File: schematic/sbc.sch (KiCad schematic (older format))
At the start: 5 parts

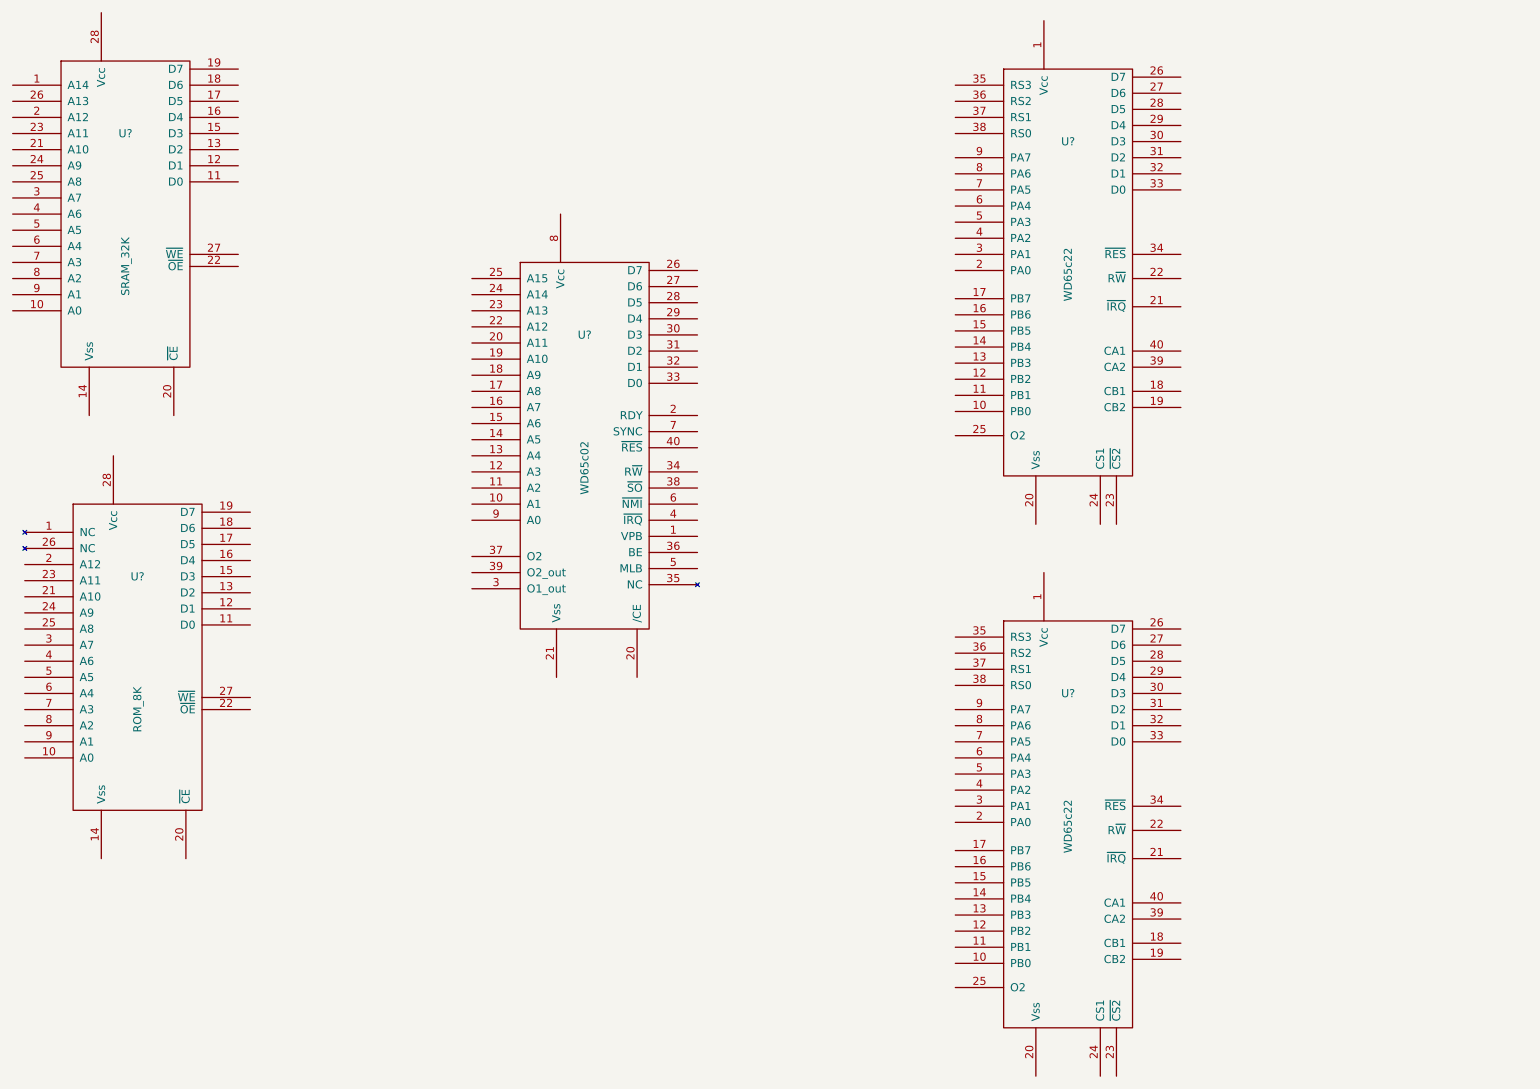
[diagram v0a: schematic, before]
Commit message: Initial SBC schematic, parts only
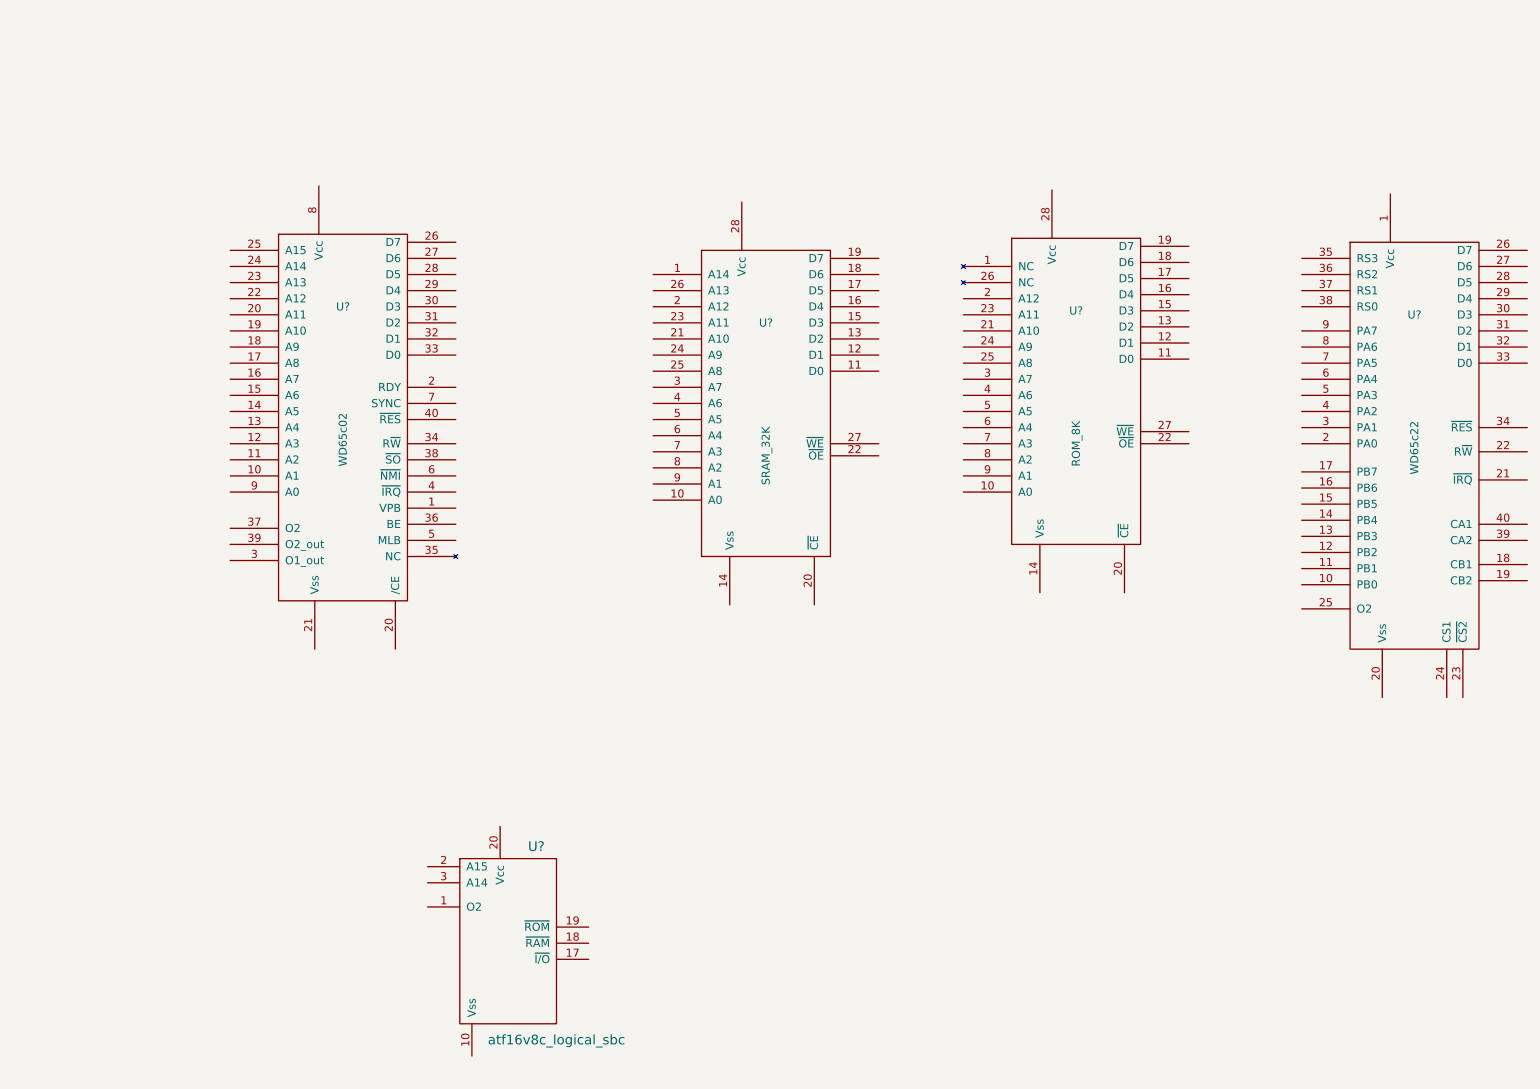
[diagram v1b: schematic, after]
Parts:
- removed U?: WD65c22, symbol WD65c22
- added U?: atf16v8c_logical_sbc, symbol atf16v8c_logical_sbc
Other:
- moved on the sheet: U?
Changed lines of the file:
@@
 L WD65c02 U?
 U 1 1 58163D7B
-P 4050 3075
-F 0 "U?" H 4050 3475 50  0000 C CNN
-F 1 "WD65c02" V 4050 2650 50  0000 C CNN
-F 2 "" H 4050 3075 50  0000 C CNN
-F 3 "" H 4050 3075 50  0000 C CNN
-	1    4050 3075
+P 2550 2900
+F 0 "U?" H 2550 3300 50  0000 C CNN
+F 1 "WD65c02" V 2550 2475 50  0000 C CNN
+F 2 "" H 2550 2900 50  0000 C CNN
+F 3 "" H 2550 2900 50  0000 C CNN
+	1    2550 2900
 	1    0    0    -1
 $EndComp
@@
 L WD65c22 U?
 U 1 1 58164F61
-P 7050 1875
-F 0 "U?" H 7050 2275 50  0000 C CNN
-F 1 "WD65c22" V 7050 1450 50  0000 C CNN
-F 2 "" H 7050 1875 50  0000 C CNN
-F 3 "" H 7050 1875 50  0000 C CNN
-	1    7050 1875
+P 9200 2950
+F 0 "U?" H 9200 3350 50  0000 C CNN
+F 1 "WD65c22" V 9200 2525 50  0000 C CNN
+F 2 "" H 9200 2950 50  0000 C CNN
+F 3 "" H 9200 2950 50  0000 C CNN
+	1    9200 2950
 	1    0    0    -1
 $EndComp
@@
 L SRAM_32K U?
 U 1 1 58165193
-P 1200 1825
-F 0 "U?" H 1200 2225 50  0000 C CNN
-F 1 "SRAM_32K" V 1200 1400 50  0000 C CNN
-F 2 "" H 1200 1825 50  0000 C CNN
-F 3 "" H 1200 1825 50  0000 C CNN
-	1    1200 1825
-	1    0    0    -1
-$EndComp
-$Comp
-L WD65c22 U?
-U 1 1 581652AF
-P 7050 5300
-F 0 "U?" H 7050 5700 50  0000 C CNN
-F 1 "WD65c22" V 7050 4875 50  0000 C CNN
-F 2 "" H 7050 5300 50  0000 C CNN
-F 3 "" H 7050 5300 50  0000 C CNN
-	1    7050 5300
+P 5175 3000
+F 0 "U?" H 5175 3400 50  0000 C CNN
+F 1 "SRAM_32K" V 5175 2575 50  0000 C CNN
+F 2 "" H 5175 3000 50  0000 C CNN
+F 3 "" H 5175 3000 50  0000 C CNN
+	1    5175 3000
 	1    0    0    -1
 $EndComp
@@
 L ROM_8K U?
 U 1 1 581659E0
-P 1275 4575
-F 0 "U?" H 1275 4975 50  0000 C CNN
-F 1 "ROM_8K" V 1275 4150 50  0000 C CNN
-F 2 "" H 1275 4575 50  0000 C CNN
-F 3 "" H 1275 4575 50  0000 C CNN
-	1    1275 4575
+P 7100 2925
+F 0 "U?" H 7100 3325 50  0000 C CNN
+F 1 "ROM_8K" V 7100 2500 50  0000 C CNN
+F 2 "" H 7100 2925 50  0000 C CNN
+F 3 "" H 7100 2925 50  0000 C CNN
+	1    7100 2925
 	1    0    0    -1
 $EndComp
+$Comp
+L atf16v8c_logical_sbc U?
+U 1 1 58164886
+P 3575 6425
+F 0 "U?" H 3750 7000 60  0000 C CNN
+F 1 "atf16v8c_logical_sbc" H 3875 5800 60  0000 C CNN
+F 2 "" H 3975 5650 60  0000 C CNN
+F 3 "" H 3975 5650 60  0000 C CNN
+	1    3575 6425
+	1    0    0    -1
+$EndComp
